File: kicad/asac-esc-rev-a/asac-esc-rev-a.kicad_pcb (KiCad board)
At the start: 2 copper layers, 29 parts, among them J14 Conn_01x03, J2 Conn_01x03, U1 AMS1117-3.3, U2 XJNG2103, U3 STM32C011F6Px, U4 ASDM30DN40E-R, DUAL MOSFET, U5 INA180A3

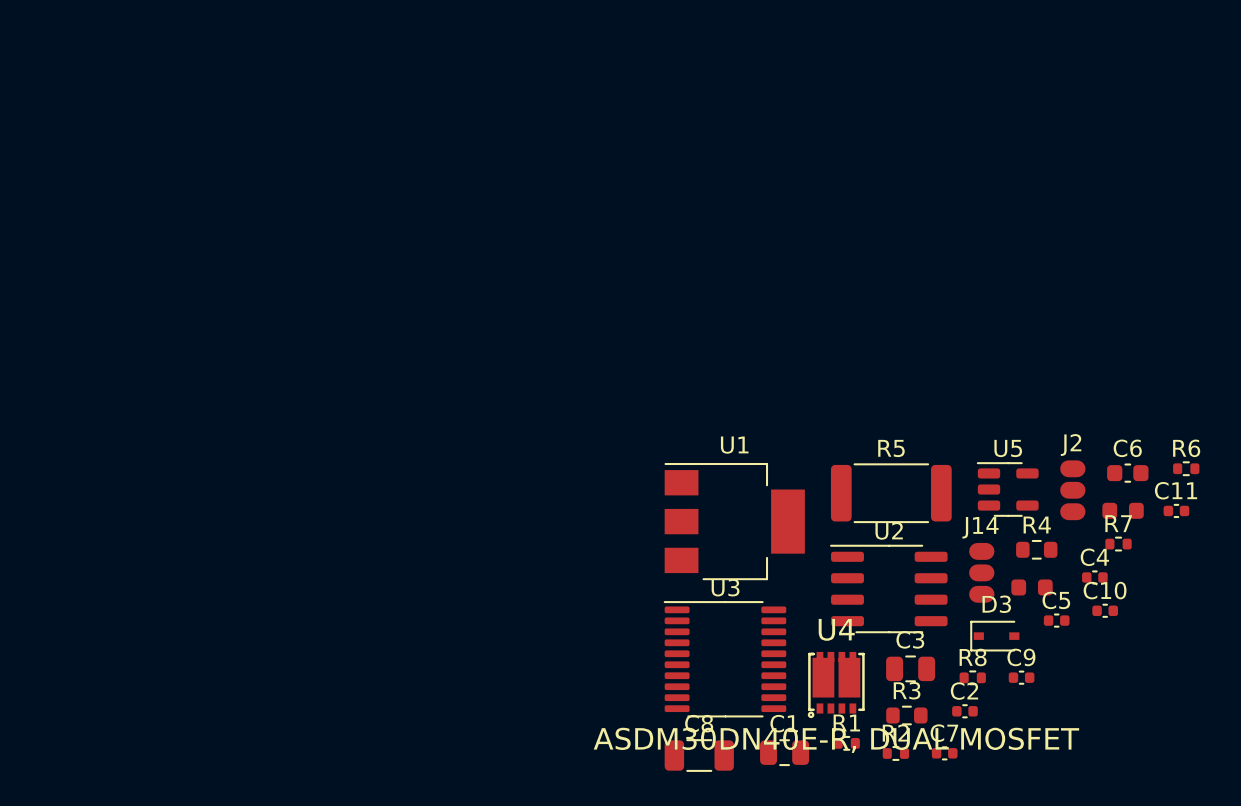
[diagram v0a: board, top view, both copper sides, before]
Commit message: Did layout and routing of PCB. Rev. A of the PCB is considered done and I have just done the order for PCB and components :)
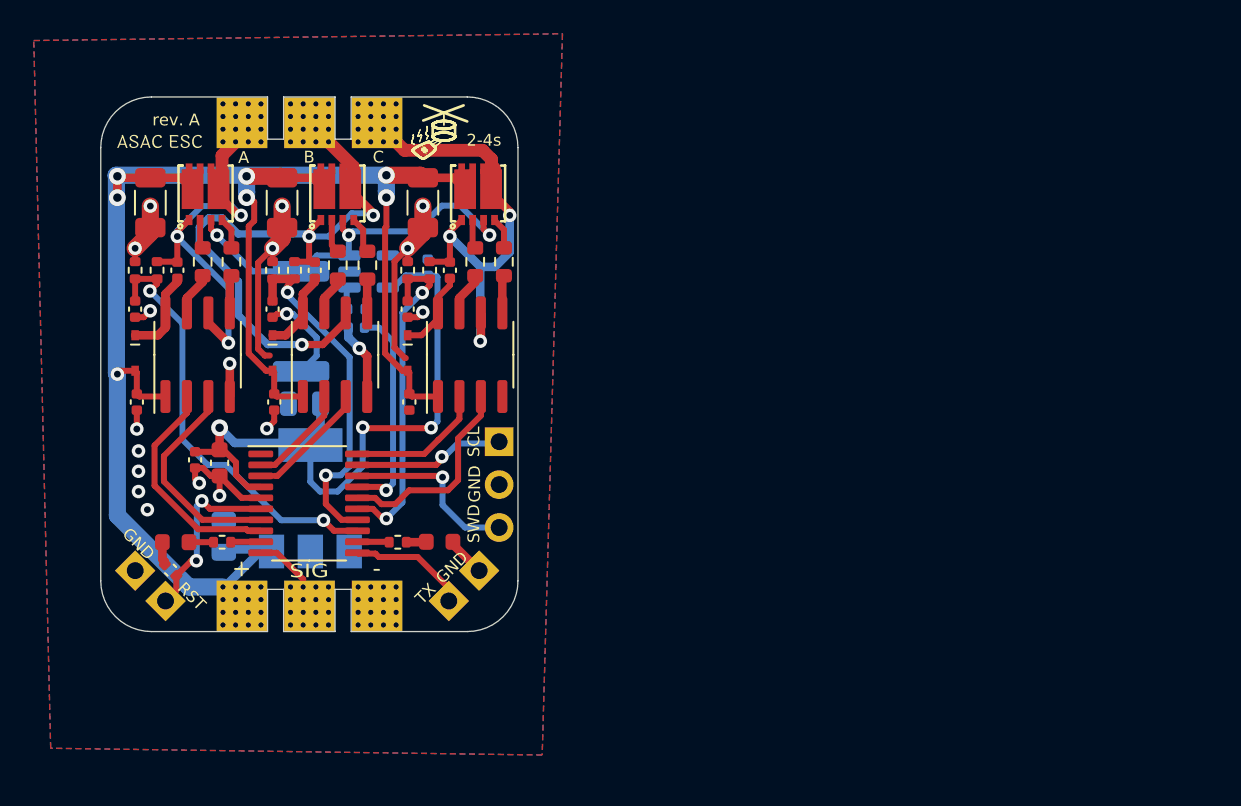
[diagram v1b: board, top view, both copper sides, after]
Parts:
- added C12: 1u, Capacitor_SMD:C_0402_1005Metric, F.Cu at (103.5, 84.5)
- added C13: 1u, Capacitor_SMD:C_0402_1005Metric, F.Cu at (105.9, 76.7)
- added C14: 47u, Capacitor_SMD:C_1206_3216Metric, F.Cu at (104.0, 72.7)
- added C15: 10n, Capacitor_SMD:C_0402_1005Metric, F.Cu at (103.4, 79.0)
- added C16: 1u, Capacitor_SMD:C_0402_1005Metric, F.Cu at (111.5, 84.5)
- added C17: 1u, Capacitor_SMD:C_0402_1005Metric, F.Cu at (113.9, 76.7)
- added C18: 47u, Capacitor_SMD:C_1206_3216Metric, F.Cu at (112.3, 72.7)
- added C19: 10n, Capacitor_SMD:C_0402_1005Metric, F.Cu at (111.4, 79.0)
- added D4: 1N5819WS, Diode_SMD:D_SOD-323, F.Cu at (103.4, 81.6)
- added D5: 1N5819WS, Diode_SMD:D_SOD-323, F.Cu at (111.4, 81.6)
- added J1: Conn_01x02_RESET, Custom:PinHeader_1x02_P2.54mm_Vertical_No_silk, F.Cu at (97.1, 96.3)
- added J3: Motor, Custom:Conn_01x03_BLDC, F.Cu at (101.5, 68.1)
- added J4: Conn_01x02_RESET, Custom:PinHeader_1x02_P2.54mm_Vertical_No_silk, F.Cu at (113.9, 96.3)
- added R10: 100R, Resistor_SMD:R_0603_1608Metric, F.Cu at (109.0, 76.4)
- added R11: 4k7, Resistor_SMD:R_0402_1005Metric, F.Cu at (104.7, 76.7)
- added R12: 1k, Resistor_SMD:R_0402_1005Metric, F.Cu at (103.4, 76.7)
- added R13: 100R, Resistor_SMD:R_0603_1608Metric, F.Cu at (115.4, 76.2)
- added R14: 100R, Resistor_SMD:R_0603_1608Metric, F.Cu at (117.1, 76.2)
- added R15: 4k7, Resistor_SMD:R_0402_1005Metric, F.Cu at (112.7, 76.7)
- added R16: 1k, Resistor_SMD:R_0402_1005Metric, F.Cu at (111.4, 76.7)
- added R9: 100R, Resistor_SMD:R_0603_1608Metric, F.Cu at (107.3, 76.4)
- added U6: XJNG2103, Package_SO:SOIC-8_3.9x4.9mm_P1.27mm, F.Cu at (107.1, 81.7)
- added U7: ASDM30DN40E-R, DUAL MOSFET, Custom:PDFN3333-8_L3.2-W3.1-P0.65-LS3.4-BL, F.Cu at (107.3, 72.2)
- added U8: XJNG2103, Package_SO:SOIC-8_3.9x4.9mm_P1.27mm, F.Cu at (115.1, 81.7)
- added U9: ASDM30DN40E-R, DUAL MOSFET, Custom:PDFN3333-8_L3.2-W3.1-P0.65-LS3.4-BL, F.Cu at (115.6, 72.2)
- C1, C10, C11, C3, R5, R6, U1, U5: moved to B.Cu
- J14: footprint Custom:PinHeader_1x03_P1.27mm_Vertical_no_silk_smd -> Custom:PinSocket_1x03_P2.54mm_Vertical_No_silk
- J2: footprint Custom:PinHeader_1x03_P1.27mm_Vertical_no_silk_smd -> Custom:Conn_01x03_BLDC
- moved C4 59.0 mm to (95.3, 79.0), turned to -90 degrees
- moved D1 56.1 mm to (97.7, 92.8)
- moved C5 56.0 mm to (97.8, 76.7), turned to 90 degrees
- moved C6 53.8 mm to (100.3, 88.1), turned to -90 degrees
- moved D3 53.7 mm to (95.3, 81.6), turned to -90 degrees
- moved R2 53.4 mm to (95.3, 76.7), turned to 90 degrees
- moved R7 53.1 mm to (100.5, 92.8)
- moved C2 52.3 mm to (95.4, 84.5), turned to 90 degrees
- moved C9 50.8 mm to (97.4, 94.5), turned to 135 degrees
- moved R4 50.6 mm to (101.0, 76.2), turned to 90 degrees
- moved R6 50.0 mm to (108.4, 79.0)
- moved J2 50.0 mm to (101.5, 96.7), turned to 90 degrees
- moved C11 49.7 mm to (108.4, 80.1), turned to 180 degrees
- moved R3 49.6 mm to (99.3, 76.2), turned to 90 degrees
- moved R1 49.5 mm to (96.6, 76.7), turned to -90 degrees
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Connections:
- J2 pad 1: SIGNAL_IN -> VCC
- J2 pad 2: VCC -> SIGNAL_IN
- R3 pad 1: /VHO_A -> Net-(R3-Pad1)
- R4 pad 1: /VLO_A -> Net-(R4-Pad1)
- U2 pad 5: /VLO_A -> Net-(R4-Pad1)
- U2 pad 7: /VHO_A -> Net-(R3-Pad1)
- U3 pad 10: unconnected-(U3-Pad10) -> SIGNAL_IN
- U3 pad 11: unconnected-(U3-Pad11) -> UART_TX
- U3 pad 12: unconnected-(U3-Pad12) -> LED_RED
- U3 pad 13: unconnected-(U3-Pad13) -> VSENSE_A
- U3 pad 14: unconnected-(U3-Pad14) -> VSENSE_B
- U3 pad 15: unconnected-(U3-Pad15) -> VSENSE_C
- U3 pad 16: unconnected-(U3-Pad16) -> ~{NLIN_C}
- U3 pad 17: unconnected-(U3-Pad17) -> CURRSENSE
- U3 pad 2: unconnected-(U3-Pad2) -> HIN_B
- U3 pad 20: unconnected-(U3-Pad20) -> HIN_C
- U3 pad 3: unconnected-(U3-Pad3) -> ~{NLIN_B}
- U3 pad 7: unconnected-(U3-Pad7) -> ~{NLIN_A}
- U3 pad 8: unconnected-(U3-Pad8) -> HIN_A
- U3 pad 9: unconnected-(U3-Pad9) -> LED_BLUE
- U4 pad 6: GND -> Net-(R5-Pad1)
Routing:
- net VCC: track 0.00 -> 101.5 mm, vias 0 -> 7
- net GND: track 0.00 -> 52.3 mm, vias 0 -> 19
- net +3.3V: track 0.00 -> 39.9 mm, vias 0 -> 3
- net B: track 0.00 -> 33.9 mm, vias 0 -> 3
- net C: track 0.00 -> 26.7 mm, vias 0 -> 3
- net VSENSE_A: track 0.00 -> 25.7 mm, vias 0 -> 2
- net Net-(R5-Pad1): track 0.00 -> 23.3 mm, vias 0 -> 3
- net A: track 0.00 -> 22.9 mm, vias 0 -> 3
- net VSENSE_B: track 0.00 -> 21.0 mm, vias 0 -> 2
- net VSENSE_C: track 0.00 -> 19.8 mm, vias 0 -> 2
- net CURRSENSE: track 0.00 -> 13.9 mm, vias 0 -> 1
- net HIN_A: track 0.00 -> 13.5 mm
- net ~{NLIN_A}: track 0.00 -> 12.8 mm
- net ~{NLIN_C}: track 0.00 -> 12.2 mm
- net ~{NRST}: track 0.00 -> 11.2 mm, vias 0 -> 2
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- added copper zone on B.Cu, net GND
- added copper zone on F.Cu, net GND
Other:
- board outline added: 24.7 x 31.7 mm
- board text added: "+"
- board text added: "-"
- board text added: "2-4s"
- board text added: "A"
- board text added: "B"
- board text added: "C"
- board text added: "GND"
- board text added: "RST"
- board text added: "SCL"
- board text added: "SIG"
- board text added: "SWD"
- board text added: "TX"
- board text added: "rev. A"
